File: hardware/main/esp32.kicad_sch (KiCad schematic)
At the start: 15 parts, among them U1 ESP32-S3-WROOM-1

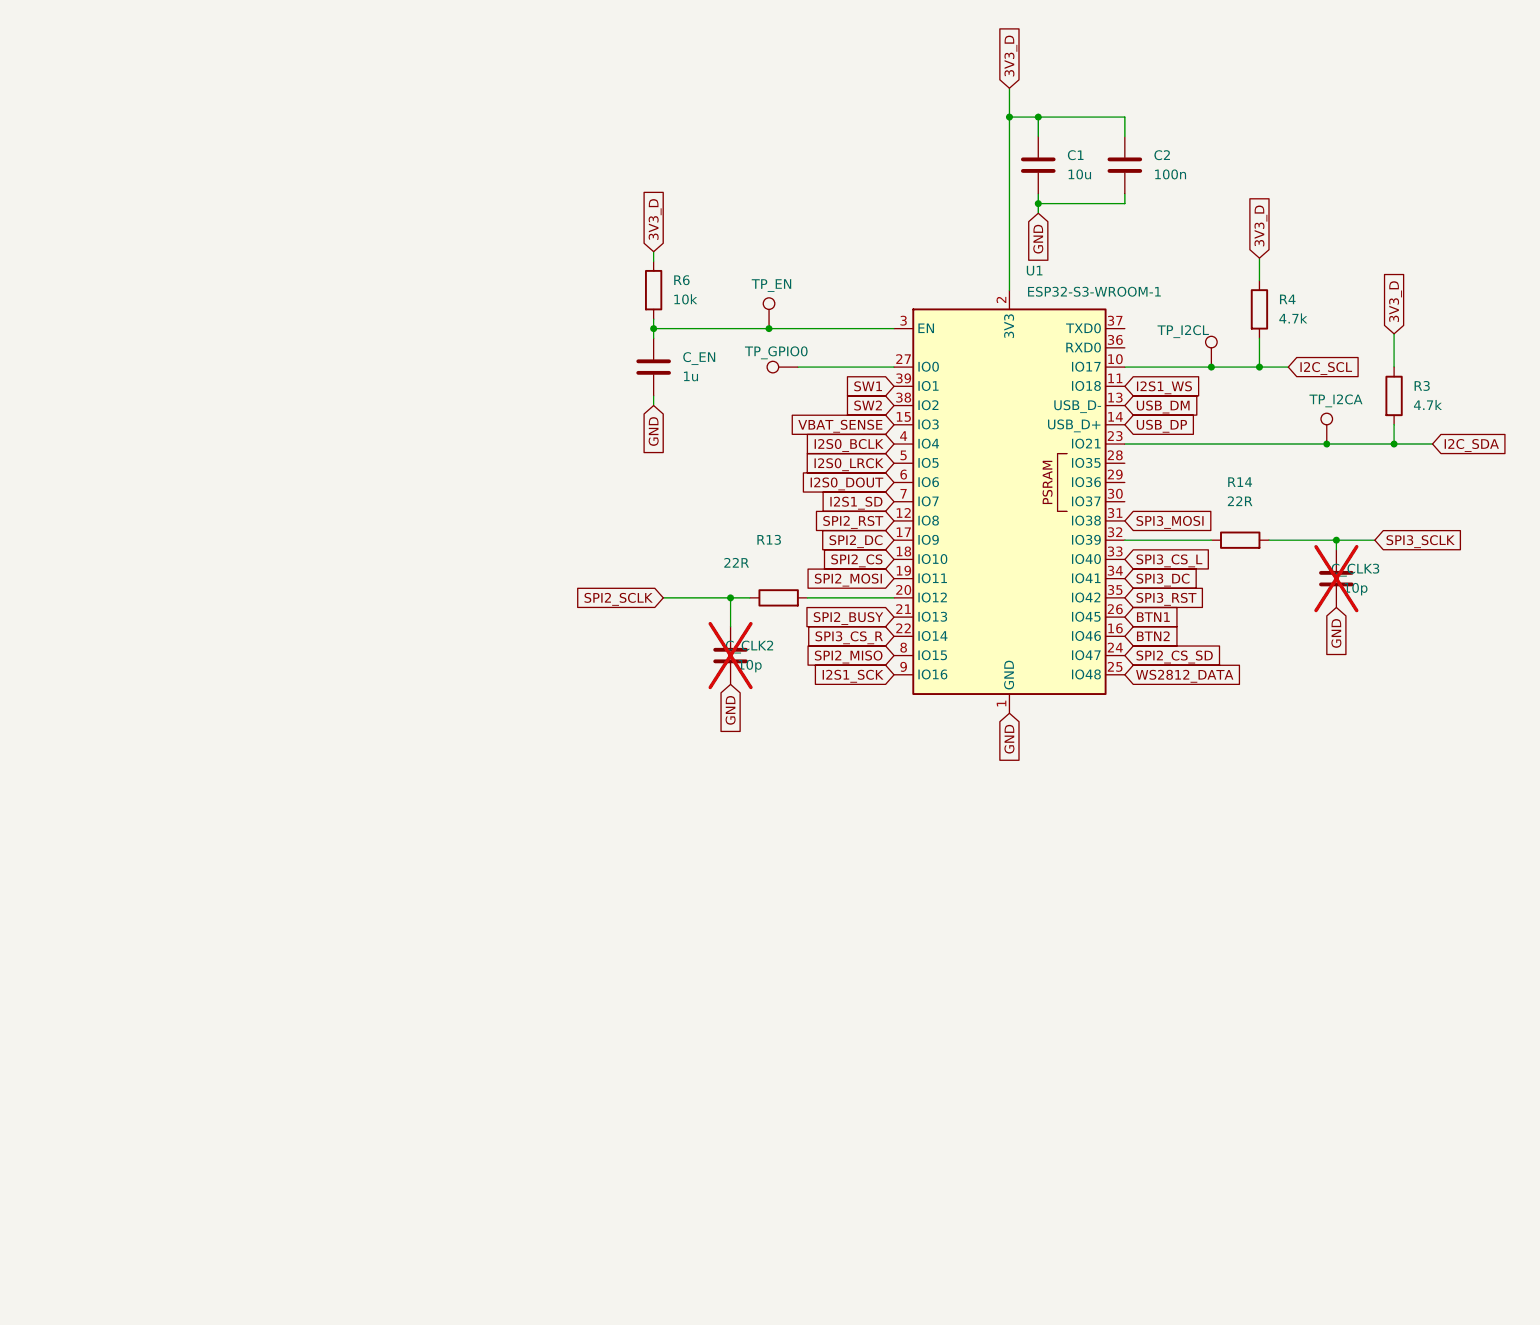
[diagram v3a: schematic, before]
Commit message: hardware: 48 erreurs ERC traitees, 22 points de test poses, VBAT_SENSE retire de J8.5
Les rapports ERC precedents portaient « Report includes: Warnings » : les
erreurs en etaient exclues a l'export et le resume affichait « Errors 0 ».
Elles etaient donc presentes depuis le debut et je ne les ai pas vues — il faut
exporter avec les erreurs incluses.

48 erreurs, trois familles, toutes des faux positifs au sens electrique mais
qu'il faut declarer sinon l'ERC reste inexploitable :

1. power_pin_not_driven (14) : le projet n'utilise aucun symbole d'alimentation,
   les rails sont des global labels, et KiCad exige qu'un net « power input »
   soit pilote par une pin « power output ». Nine PWR_FLAG poses, un par rail
   (GND, VSYS, VBAT, VBAT-, 3V3_D, 3V3_A, 5V, 5V_BOOST, 5V_USB).
2. pin_not_connected (29) : broches volontairement libres — paires SuperSpeed et
   SBU de l'USB-C (design USB 2.0), UART0 et IO35-37 de l'ESP32 (reserves a la
   PSRAM octale), GPIO du PCM5122, interruptions de l'IMU, reserves de
   connecteurs, drains communs du FS8205. Marqueurs no_connect.
3. divers (5) : label GND orphelin hors page (122, 228.81 — la page fait
   210 mm de haut) supprime ; C1_AV/C2_DV/C3_CP renommes C_AVDD/C_DVDD/C_CPVDD
   (KiCad lit « C1_AV » comme un prefixe suivi de « 1_AV », donc non annote) ;
   OUT_11 du bq24075 passee en passive (les deux broches sont la meme sortie).

Points de test : les 22 valides sont poses, chacun relie par un fil court a un
global label (le routeur les placera ou ils sont accessibles). 22/22 verifies
sur leur net. Trois nets anonymes nommes au passage : BQ_ISET, BQ_CHG,
BOOST_FB. Avec les 4 existants, 26 points de test.

VBAT_SENSE retire de J8.5 : noeud ADC haute impedance (1M // 1M) sorti dans un
cable, sans usage cote face avant depuis que les analogiques passent par
l'ADS7830. Broche marquee non connectee.

CORRECTION D'OUTIL : tools/kicad_netlist.py comptait PWR_FLAG comme un nom de
net, ce qui faisait fusionner les neuf rails en un seul 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
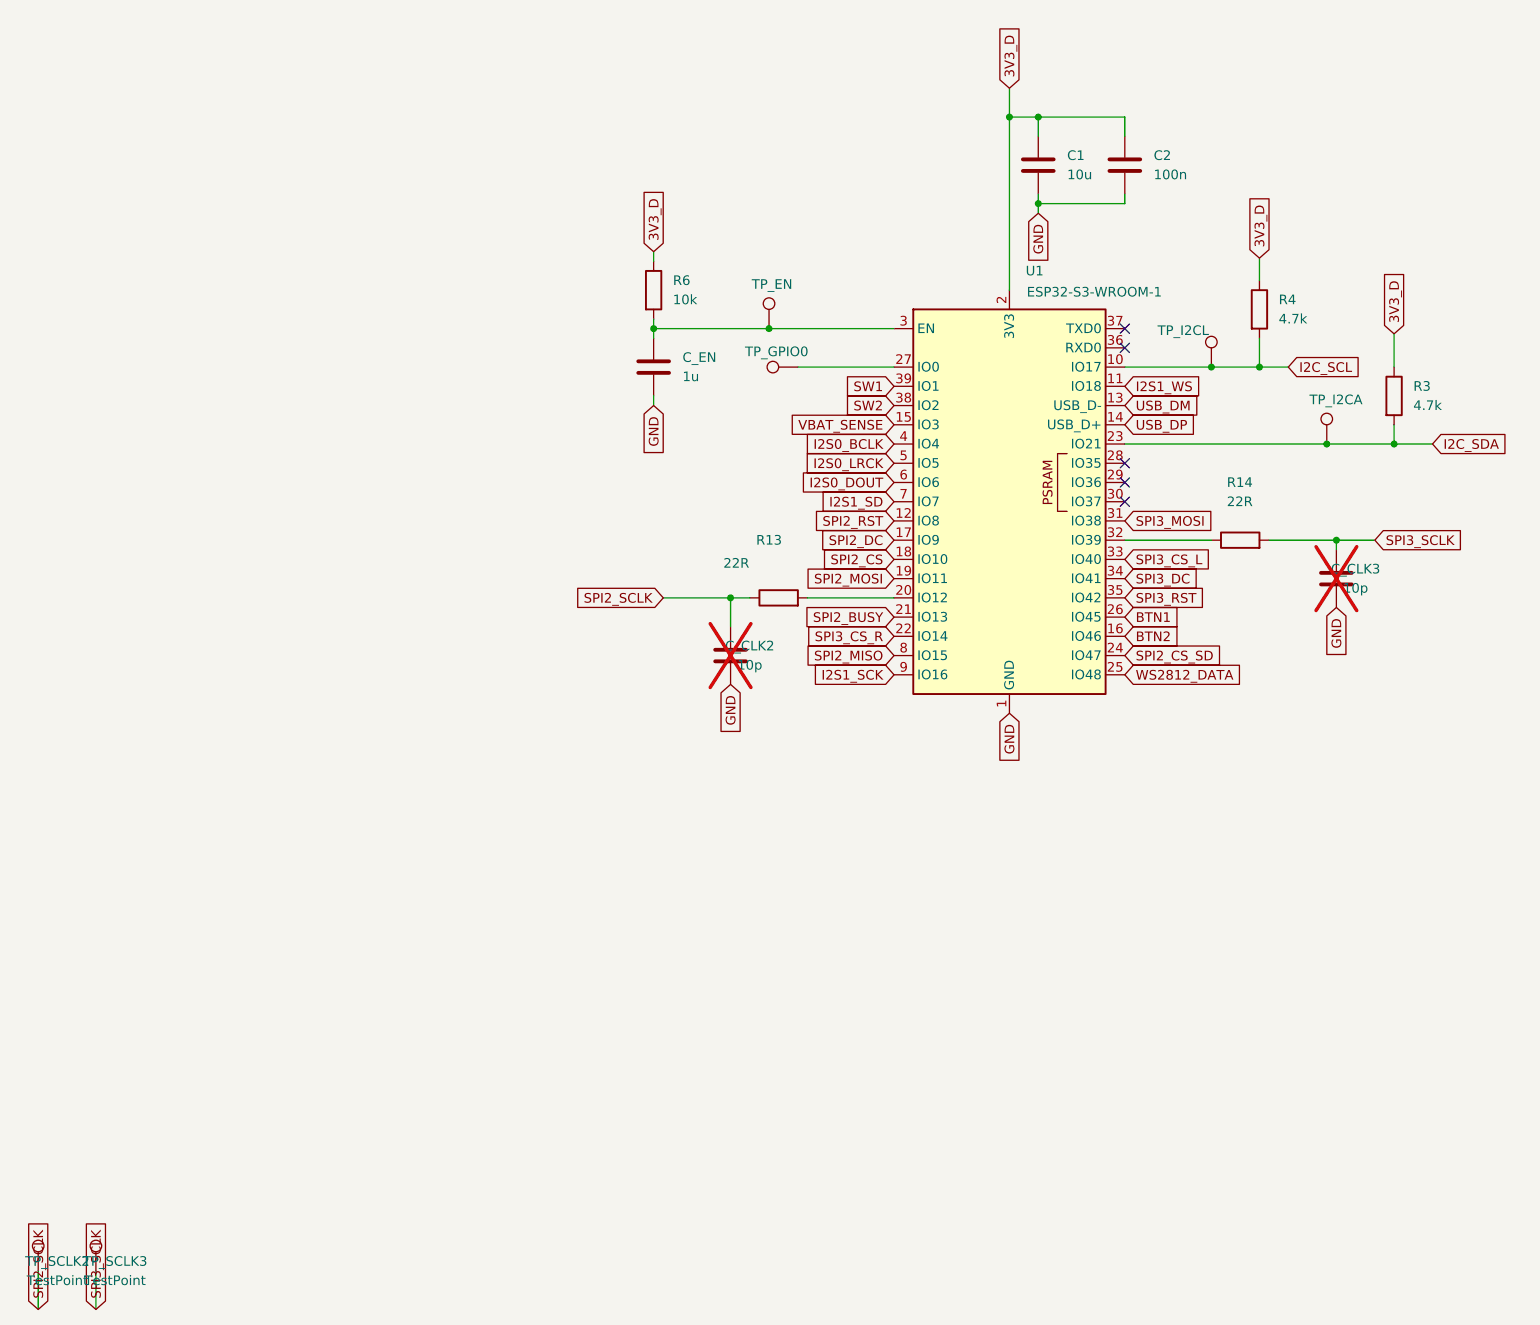
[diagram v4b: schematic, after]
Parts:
- added TP_SCLK2, TP_SCLK3: TestPoint, TestPoint:TestPoint_Pad_D1.5mm, symbol Connector:TestPoint
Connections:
- net SPI2_SCLK: now also TP_SCLK2.1
- net SPI3_SCLK: now also TP_SCLK3.1
- no-connect marks 0 -> 5
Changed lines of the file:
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@@
+		)
+	)
+	(no_connect
+		(at 161.29 69.85)
+	)
+	(no_connect
+		(at 161.29 67.31)
+	)
+	(no_connect
+		(at 161.29 85.09)
+	)
+	(no_connect
+		(at 161.29 87.63)
+	)
+	(no_connect
+		(at 161.29 90.17)
+	)
+	(symbol
+		(lib_id "Connector:TestPoint")
+		(at 17.78 191.77 0)
+		(unit 1)
+		(body_style 1)
+		(exclude_from_sim no)
+		(in_bom yes)
+		(on_board yes)
+		(in_pos_files yes)
+		(dnp no)
+		(property "Reference" "TP_SCLK2"
+			(at 20.32 190.5 0)
+			(show_name no)
+			(do_not_autoplace no)
+			(effects
+				(font
+					(size 1.27 1.27)
+				)
+			)
+		)
+		(property "Value" "TestPoint"
+			(at 20.32 193.04000000000002 0)
+			(show_name no)
+			(do_not_autoplace no)
+			(effects
+				(font
+					(size 1.27 1.27)
+				)
+			)
+		)
+		(property "Footprint" "TestPoint:TestPoint_Pad_D1.5mm"
+			(at 17.78 191.77 0)
+			(hide yes)
+			(show_name no)
+			(do_not_autoplace no)
+			(effects
+				(font
+					(size 1.27 1.27)
+				)
+			)
+		)
+		(property "Datasheet" ""
+			(at 17.78 191.77 0)
+			(hide yes)
+			(show_name no)
+			(do_not_autoplace no)
+			(effects
+				(font
+					(size 1.27 1.27)
+				)
+			)
+		)
+		(property "Description" "Point de test SPI2_SCLK — voir docs/pcb/03-validation-qualite.md"
+			(at 17.78 191.77 0)
+			(hide yes)
+			(show_name no)
+			(do_not_autoplace no)
+			(effects
+				(font
+					(size 1.27 1.27)
+				)
+			)
+		)
+		(pin "1"
+		)
+		(instances
+			(project "blackbox"
+				(path "/49e0257f-ff47-4890-a1ac-89438fa62044/14cfff57-6a31-4c05-af76-83111480b025"
+					(reference "TP_SCLK2")
+					(unit 1)
+				)
+			)
+		)
+	)
+	(wire
+		(pts
+			(xy 17.78 191.77) (xy 17.78 196.85000000000002)
+		)
+		(stroke
+			(width 0)
+			(type default)
+		)
+	)
+	(global_label "SPI2_SCLK"
+		(shape input)
+		(at 17.78 196.85000000000002 270)
+		(fields_autoplaced yes)
+		(effects
+			(font
+				(size 1.27 1.27)
+			)
+			(justify left)
+		)
+		(property "Intersheetrefs" "${INTERSHEET_REFS}"
+			(at 29.21 196.85000000000002 0)
+			(hide yes)
+			(show_name no)
+			(do_not_autoplace no)
+			(effects
+				(font
+					(size 1.27 1.27)
+				)
+				(justify left)
+			)
+		)
+	)
+	(symbol
+		(lib_id "Connector:TestPoint")
+		(at 25.4 191.77 0)
+		(unit 1)
+		(body_style 1)
+		(exclude_from_sim no)
+		(in_bom yes)
+		(on_board yes)
+		(in_pos_files yes)
+		(dnp no)
+		(property "Reference" "TP_SCLK3"
+			(at 27.939999999999998 190.5 0)
+			(show_name no)
+			(do_not_autoplace no)
+			(effects
+				(font
+					(size 1.27 1.27)
+				)
+			)
+		)
+		(property "Value" "TestPoint"
+			(at 27.939999999999998 193.04000000000002 0)
+			(show_name no)
+			(do_not_autoplace no)
+			(effects
+				(font
+					(size 1.27 1.27)
+				)
+			)
+		)
+		(property "Footprint" "TestPoint:TestPoint_Pad_D1.5mm"
+			(at 25.4 191.77 0)
+			(hide yes)
+			(show_name no)
+			(do_not_autoplace no)
+			(effects
+				(font
+					(size 1.27 1.27)
+				)
+			)
+		)
+		(property "Datasheet" ""
+			(at 25.4 191.77 0)
+			(hide yes)
+			(show_name no)
+			(do_not_autoplace no)
+			(effects
+				(font
+					(size 1.27 1.27)
+				)
+			)
+		)
+		(property "Description" "Point de test SPI3_SCLK — voir docs/pcb/03-validation-qualite.md"
+			(at 25.4 191.77 0)
+			(hide yes)
+			(show_name no)
+			(do_not_autoplace no)
+			(effects
+				(font
+					(size 1.27 1.27)
+				)
+			)
+		)
+		(pin "1"
+		)
+		(instances
+			(project "blackbox"
+				(path "/49e0257f-ff47-4890-a1ac-89438fa62044/14cfff57-6a31-4c05-af76-83111480b025"
+					(reference "TP_SCLK3")
+					(unit 1)
+				)
+			)
+		)
+	)
+	(wire
+		(pts
+			(xy 25.4 191.77) (xy 25.4 196.85000000000002)
+		)
+		(stroke
+			(width 0)
+			(type default)
+		)
+	)
+	(global_label "SPI3_SCLK"
+		(shape input)
+		(at 25.4 196.85000000000002 270)
+		(fields_autoplaced yes)
+		(effects
+			(font
+				(size 1.27 1.27)
+			)
+			(justify left)
+		)
+		(property "Intersheetrefs" "${INTERSHEET_REFS}"
+			(at 36.83 196.85000000000002 0)
+			(hide yes)
+			(show_name no)
+			(do_not_autoplace no)
+			(effects
+				(font
+					(size 1.27 1.27)
+				)
+				(justify left)
+			)
 		)
 	)

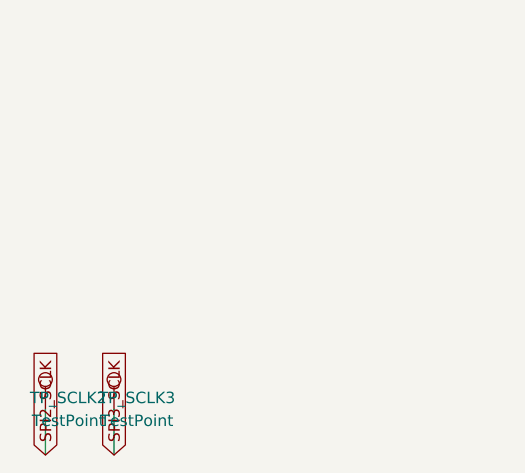
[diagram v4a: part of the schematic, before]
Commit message: datasheets: ATtiny1616, reference documentaire non inventee
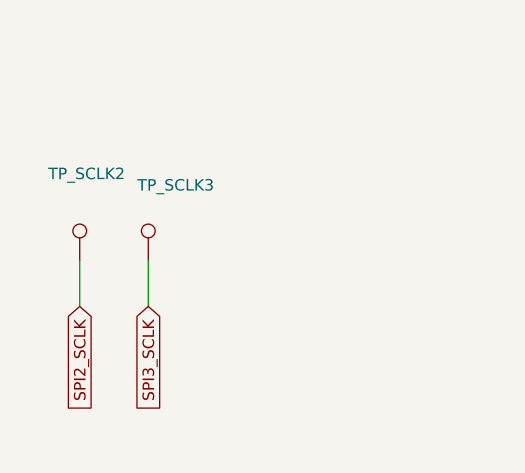
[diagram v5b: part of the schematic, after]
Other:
- moved on the sheet: TP_SCLK2, TP_SCLK3

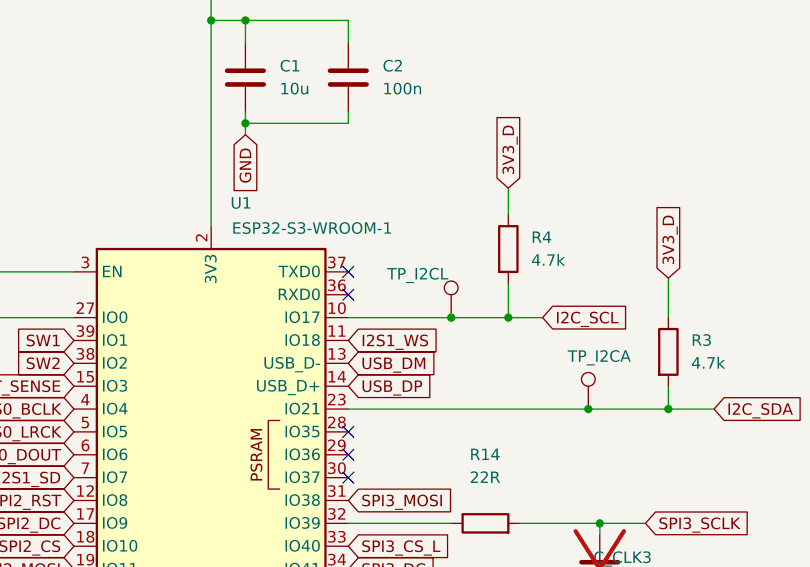
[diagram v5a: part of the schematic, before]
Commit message: main: pastilles UART0 TP_TXD0/TP_RXD0 ; SW3 cable en direct sur J12 (modele a rechoisir)
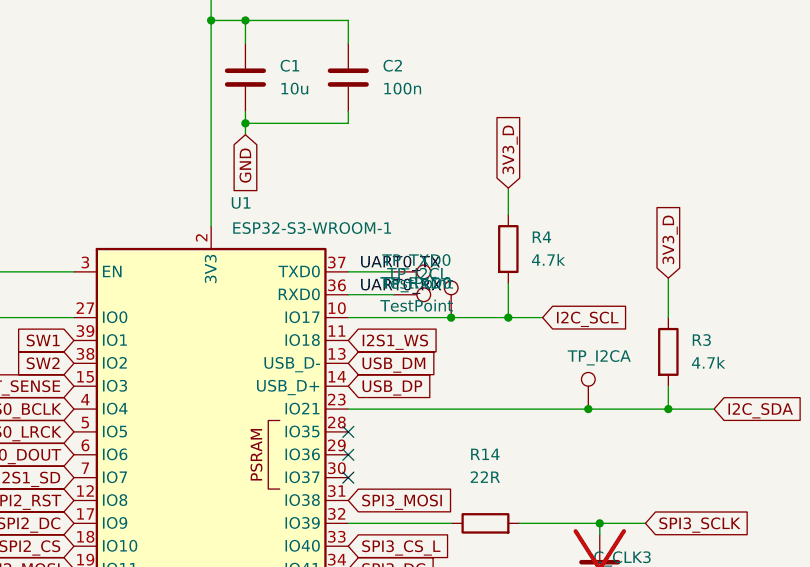
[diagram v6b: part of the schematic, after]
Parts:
- added TP_RXD0, TP_TXD0: TestPoint, TestPoint:TestPoint_Pad_D1.5mm, symbol Connector:TestPoint
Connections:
- net UART0_RX: now reaches U1.36 (RXD0)
- net UART0_RX: now also TP_RXD0.1
- net UART0_TX: now reaches U1.37 (TXD0)
- net UART0_TX: now also TP_TXD0.1
- no-connect marks 5 -> 3
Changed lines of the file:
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@@
-	)
-	(no_connect
-		(at 161.29 69.85)
-	)
-	(no_connect
-		(at 161.29 67.31)
 	)
 	(no_connect
@@
 		)
 	)
+	(symbol
+		(lib_id "Connector:TestPoint")
+		(at 166.37 67.31 270)
+		(unit 1)
+		(body_style 1)
+		(exclude_from_sim no)
+		(in_bom yes)
+		(on_board yes)
+		(in_pos_files yes)
+		(dnp no)
+		(property "Reference" "TP_TXD0"
+			(at 168.91 66.04 270)
+			(show_name no)
+			(do_not_autoplace no)
+			(effects
+				(font
+					(size 1.27 1.27)
+				)
+			)
+		)
+		(property "Value" "TestPoint"
+			(at 168.91 68.58 270)
+			(show_name no)
+			(do_not_autoplace no)
+			(effects
+				(font
+					(size 1.27 1.27)
+				)
+			)
+		)
+		(property "Footprint" "TestPoint:TestPoint_Pad_D1.5mm"
+			(at 166.37 67.31 270)
+			(hide yes)
+			(show_name no)
+			(do_not_autoplace no)
+			(effects
+				(font
+					(size 1.27 1.27)
+				)
+			)
+		)
+		(property "Datasheet" ""
+			(at 166.37 67.31 0)
+			(hide yes)
+			(show_name no)
+			(do_not_autoplace no)
+			(effects
+				(font
+					(size 1.27 1.27)
+				)
+			)
+		)
+		(property "Description" "Console UART0 : TX de la box (pin 37 du module) — adaptateur USB-serie 3,3 V"
+			(at 166.37 67.31 0)
+			(hide yes)
+			(show_name no)
+			(do_not_autoplace no)
+			(effects
+				(font
+					(size 1.27 1.27)
+				)
+			)
+		)
+		(pin "1"
+		)
+		(instances
+			(project "blackbox"
+				(path "/49e0257f-ff47-4890-a1ac-89438fa62044/14cfff57-6a31-4c05-af76-83111480b025"
+					(reference "TP_TXD0")
+					(unit 1)
+				)
+			)
+		)
+	)
+	(wire
+		(pts
+			(xy 161.29 67.31) (xy 166.37 67.31)
+		)
+		(stroke
+			(width 0)
+			(type default)
+		)
+	)
+	(symbol
+		(lib_id "Connector:TestPoint")
+		(at 166.37 69.85 270)
+		(unit 1)
+		(body_style 1)
+		(exclude_from_sim no)
+		(in_bom yes)
+		(on_board yes)
+		(in_pos_files yes)
+		(dnp no)
+		(property "Reference" "TP_RXD0"
+			(at 168.91 68.58 270)
+			(show_name no)
+			(do_not_autoplace no)
+			(effects
+				(font
+					(size 1.27 1.27)
+				)
+			)
+		)
+		(property "Value" "TestPoint"
+			(at 168.91 71.11999999999999 270)
+			(show_name no)
+			(do_not_autoplace no)
+			(effects
+				(font
+					(size 1.27 1.27)
+				)
+			)
+		)
+		(property "Footprint" "TestPoint:TestPoint_Pad_D1.5mm"
+			(at 166.37 69.85 270)
+			(hide yes)
+			(show_name no)
+			(do_not_autoplace no)
+			(effects
+				(font
+					(size 1.27 1.27)
+				)
+			)
+		)
+		(property "Datasheet" ""
+			(at 166.37 69.85 0)
+			(hide yes)
+			(show_name no)
+			(do_not_autoplace no)
+			(effects
+				(font
+					(size 1.27 1.27)
+				)
+			)
+		)
+		(property "Description" "Console UART0 : RX de la box (pin 36 du module) — adaptateur USB-serie 3,3 V"
+			(at 166.37 69.85 0)
+			(hide yes)
+			(show_name no)
+			(do_not_autoplace no)
+			(effects
+				(font
+					(size 1.27 1.27)
+				)
+			)
+		)
+		(pin "1"
+		)
+		(instances
+			(project "blackbox"
+				(path "/49e0257f-ff47-4890-a1ac-89438fa62044/14cfff57-6a31-4c05-af76-83111480b025"
+					(reference "TP_RXD0")
+					(unit 1)
+				)
+			)
+		)
+	)
+	(wire
+		(pts
+			(xy 161.29 69.85) (xy 166.37 69.85)
+		)
+		(stroke
+			(width 0)
+			(type default)
+		)
+	)
+	(label "UART0_TX"
+		(at 162.56 67.31 0)
+		(fields_autoplaced yes)
+		(effects
+			(font
+				(size 1.27 1.27)
+			)
+			(justify left bottom)
+		)
+	)
+	(label "UART0_RX"
+		(at 162.56 69.85 0)
+		(fields_autoplaced yes)
+		(effects
+			(font
+				(size 1.27 1.27)
+			)
+			(justify left bottom)
+		)
+	)
